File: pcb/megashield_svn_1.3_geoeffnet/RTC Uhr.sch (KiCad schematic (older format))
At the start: 1 part, among them U8 DS1307+

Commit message: Platine V1.3
Hierarchischer Schaltplan für Step Down Wandler erstellt
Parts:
- U8: footprint (none) -> ACS712:Tiny_RTC_DS1307_geändert_mit_Bohrloch_4Lochreihen
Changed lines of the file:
@@
 EESchema Schematic File Version 2
+LIBS:Lötpad_2,5mm
 LIBS:power
 LIBS:Bluetooth_ZS_HC_05
@@
 $Descr A4 11693 8268
 encoding utf-8
-Sheet 12 16
+Sheet 12 17
 Title "Ardumower shield SVN Version 1.3"
 Date "Sonntag, 26. April 2015"
 Rev "1.3"
-Comp " by UweZ"
-Comment1 ""
+Comp "von UweZ"
+Comment1 "RTC Uhr"
 Comment2 ""
 Comment3 ""
@@
 F 0 "U8" H 5395 3200 60  0000 C CNN
 F 1 "DS1307+" H 5395 3005 60  0000 C CNN
-F 2 "" H 5395 3070 60  0000 C CNN
+F 2 "ACS712:Tiny_RTC_DS1307_geändert_mit_Bohrloch_4Lochreihen" H 5395 3070 60  0001 C CNN
 F 3 "" H 5395 3070 60  0000 C CNN
 F 4 "Value" H 5395 3070 60  0001 C CNN "Bestellnummer"
@@
 $EndComp
 $Comp
-L +5V #PWR0111
+L +5V #PWR098
 U 1 1 5540D156
 P 5395 2410
-F 0 "#PWR0111" H 5395 2260 60  0001 C CNN
+F 0 "#PWR098" H 5395 2260 60  0001 C CNN
 F 1 "+5V" H 5395 2550 60  0000 C CNN
 F 2 "" H 5395 2410 60  0000 C CNN
@@
 	5395 2470 5395 2410
 $Comp
-L GND #PWR0112
+L GND #PWR099
 U 1 1 5540D459
 P 5395 3790
-F 0 "#PWR0112" H 5395 3540 60  0001 C CNN
+F 0 "#PWR099" H 5395 3540 60  0001 C CNN
 F 1 "GND" H 5395 3640 60  0000 C CNN
 F 2 "" H 5395 3790 60  0000 C CNN

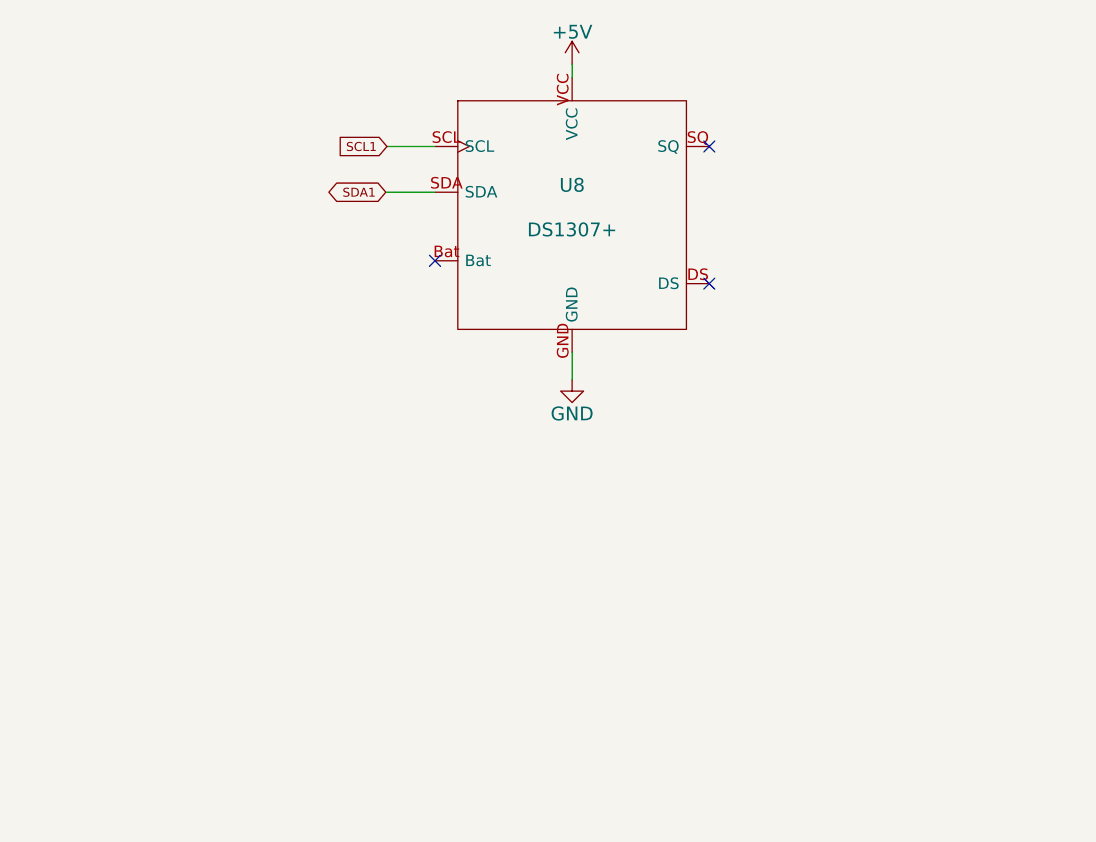
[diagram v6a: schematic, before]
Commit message: Platine V1.3
RTC Uhr und INA169 Uhr hinzugefügt
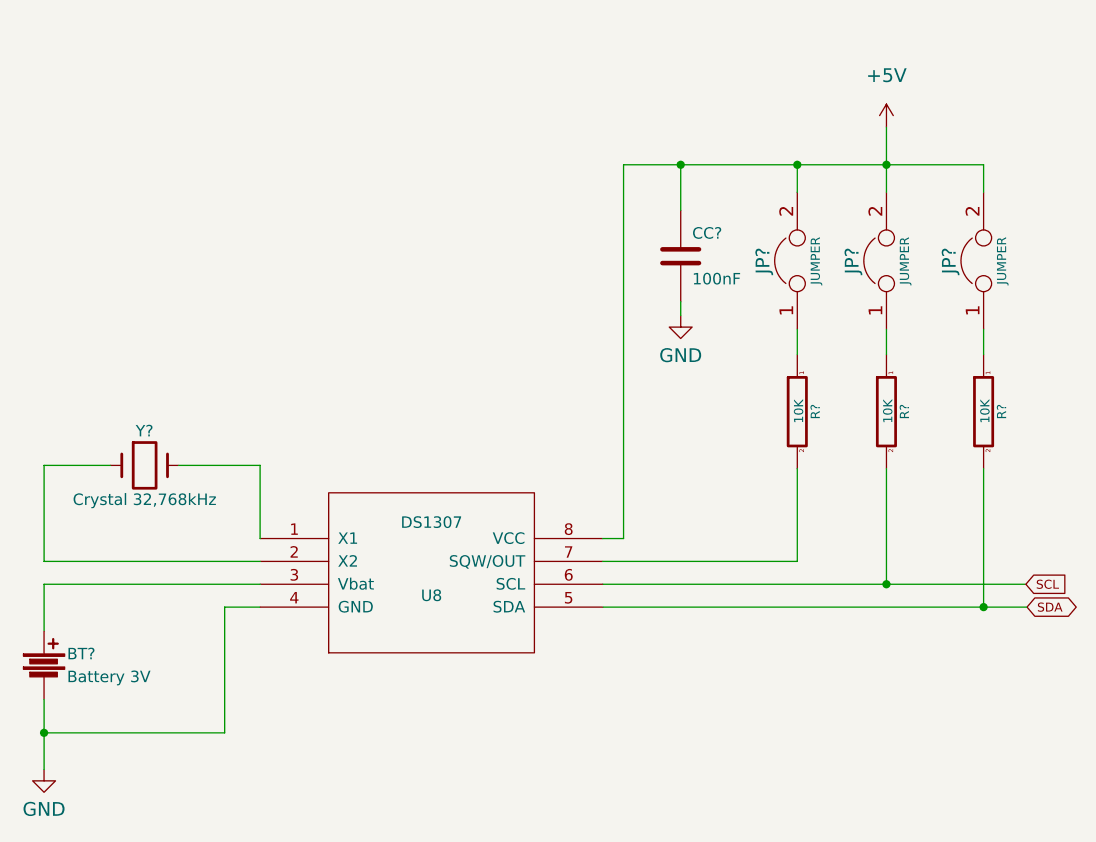
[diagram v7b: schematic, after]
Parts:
- removed U8: DS1307+, ACS712:Tiny_RTC_DS1307_geändert_mit_Bohrloch_4Lochreihen, symbol DS1307+
- added BT?: Battery 3V, symbol Battery
- added CC?: 100nF, symbol C
- added JP? (x3): JUMPER, symbol JUMPER
- added R? (x3): 10K, symbol R
- added U8: DS1307, MODULE, symbol DS1307
- added Y?: Crystal 32,768kHz, symbol Crystal
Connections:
- net +5V: now also CC?.1, JP?.2, JP?.2, JP?.2, U8.8 (VCC)
- net GND: now also BT?.2, CC?.2, U8.4 (GND)
- new net: U8.1 (X1), Y?.2
- new net: U8.2 (X2), Y?.1
- new net: BT?.1, U8.3 (Vbat)
- new net: R?.2, U8.7 (SQW/OUT)
- new net: JP?.1, R?.1 (x3)
- new net SCL: R?.2, U8.6 (SCL)
- new net SDA: R?.2, U8.5 (SDA)
- no-connect marks 3 -> 0
